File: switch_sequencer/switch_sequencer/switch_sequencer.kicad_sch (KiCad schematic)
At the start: 14 parts, among them SW1 SW_MEC_5G_LED, U4 pico, U5 TMUX4051PWR

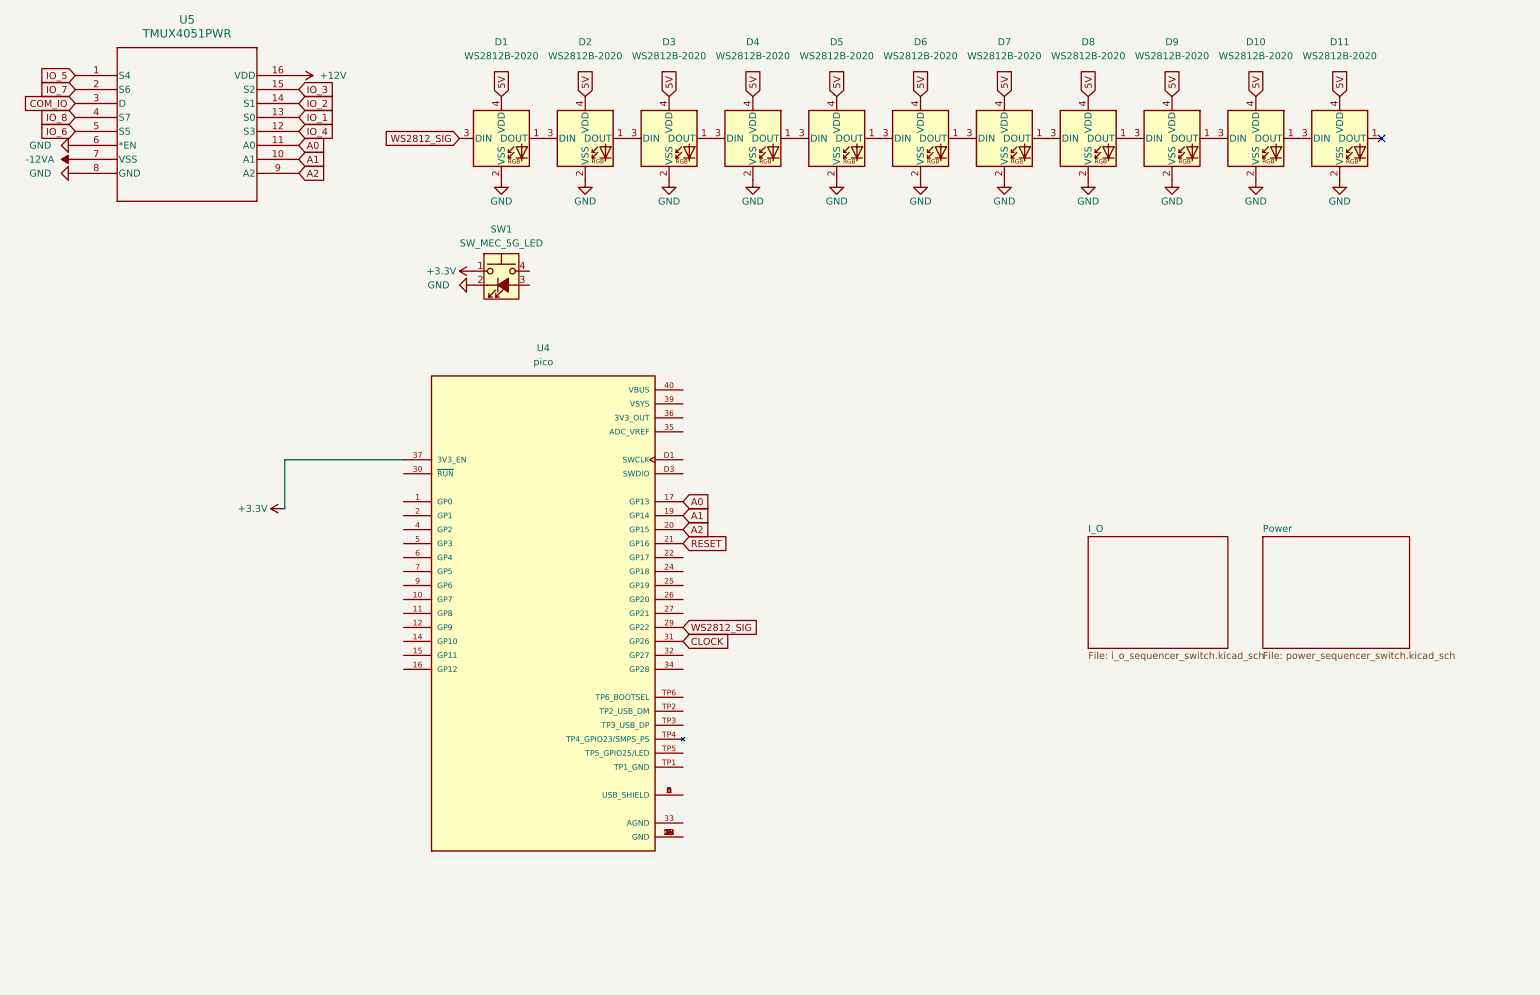
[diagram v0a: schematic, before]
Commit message: Reformated folder structure. Finished layout of sample and hold.
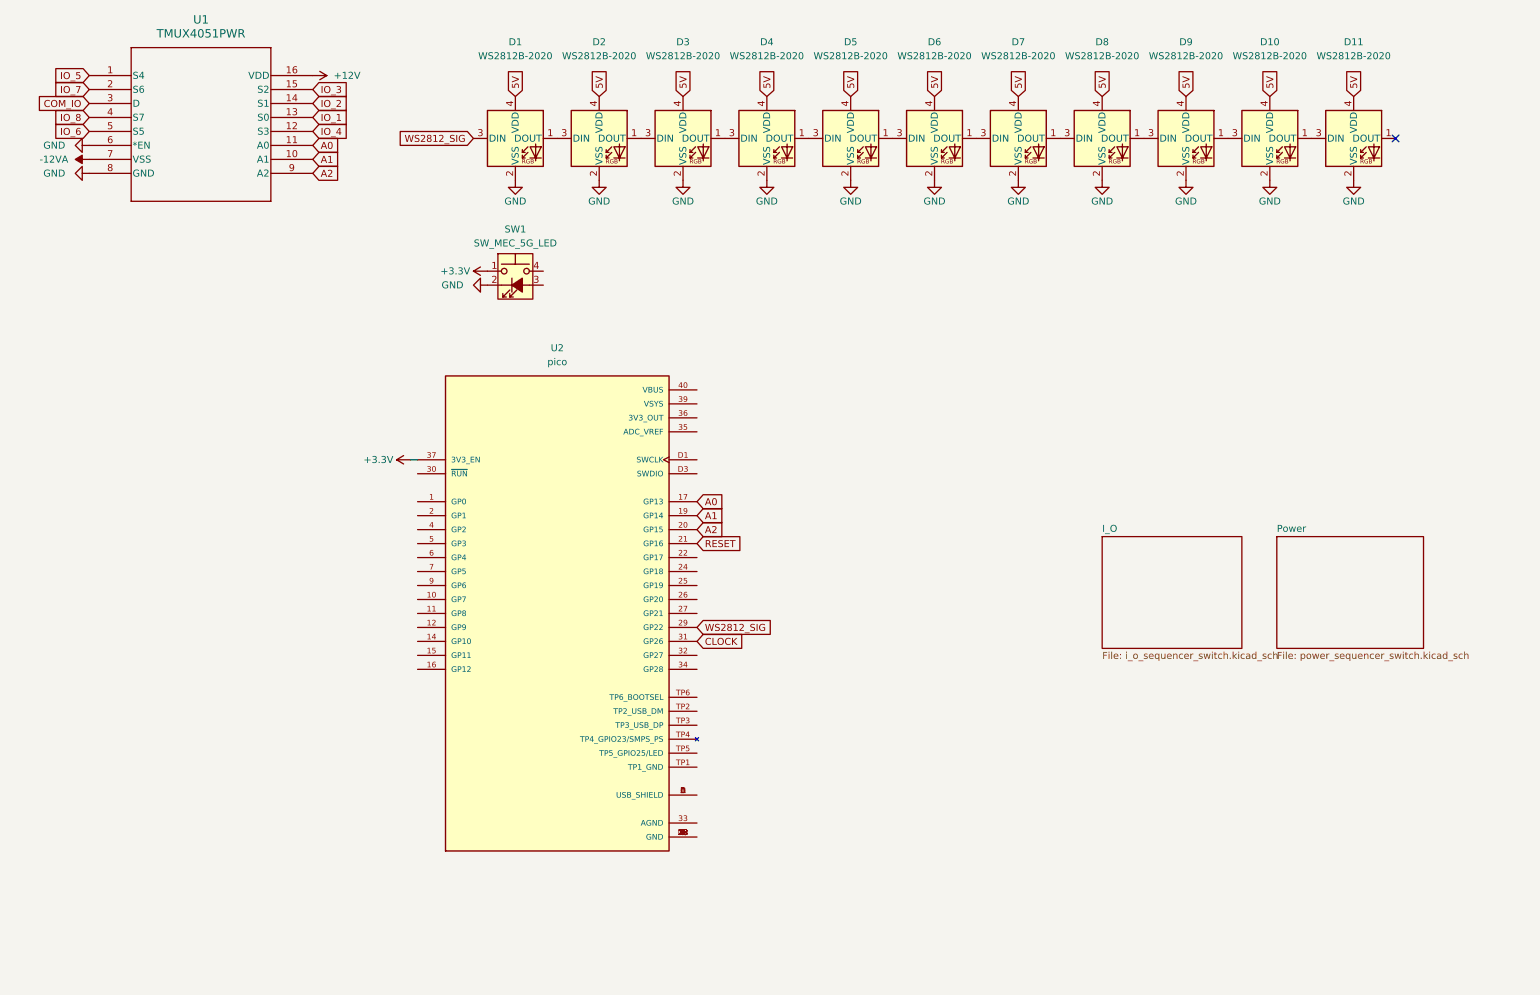
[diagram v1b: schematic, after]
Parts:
- removed U4: pico, SC0915:MODULE_SC0915, symbol pico:pico
- removed U5: TMUX4051PWR, TMUX4051:TSSOP16_PW_TEX, symbol TMUX4051:TMUX4051PWR
- added U1: TMUX4051PWR, TMUX4051:TSSOP16_PW_TEX, symbol TMUX4051:TMUX4051PWR
- added U2: pico, SC0915:MODULE_SC0915, symbol pico:pico
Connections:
- net +12V: now also U1.16 (VDD)
- net +3.3V: now also U2.37 (3V3_EN)
- net -12VA: now also U1.7 (VSS)
- net A0: now also U1.11 (A0), U2.17 (GP13)
- net A1: now also U1.10 (A1), U2.19 (GP14)
- net A2: now also U1.9 (A2), U2.20 (GP15)
- net CLOCK: now also U2.31 (GP26)
- net COM_IO: now also U1.3 (D)
- net GND: now also U1.6 (*EN), U1.8 (GND)
- net IO_1: now also U1.13 (S0)
- net IO_2: now also U1.14 (S1)
- net IO_3: now also U1.15 (S2)
- net IO_4: now also U1.12 (S3)
- net IO_5: now also U1.1 (S4)
- net IO_6: now also U1.5 (S5)
- net IO_7: now also U1.2 (S6)
- net IO_8: now also U1.4 (S7)
- net RESET: now also U2.21 (GP16)
- net WS2812_SIG: now also U2.29 (GP22)
- new net: U2.13 (GND), U2.18 (GND), U2.23 (GND), U2.28 (GND), U2.3 (GND), U2.38 (GND), U2.8 (GND), U2.D2 (GND)
- new net: U2.A (USB_SHIELD), U2.B (USB_SHIELD), U2.C (USB_SHIELD), U2.D (USB_SHIELD)

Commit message: sequential switch wip
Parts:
- removed D1, D10, D11, D2, D3, D4, D5, D6, D7, D8, D9: WS2812B-2020, LED_SMD:LED_WS2812B-2020_PLCC4_2.0x2.0mm, symbol LED:WS2812B-2020
- removed SW1: SW_MEC_5G_LED, symbol Switch:SW_MEC_5G_LED
- removed U1: TMUX4051PWR, TMUX4051:TSSOP16_PW_TEX, symbol TMUX4051:TMUX4051PWR
- removed U2: pico, SC0915:MODULE_SC0915, symbol pico:pico
- added J1, J2: 3.5mm_Mono_Switched_sm, 4ms_Jack:EighthInch_PJ398SM, symbol 4ms_Jack:3.5mm_Mono_Switched_sm
- added J12: Conn_01x03, 4ms_Connector:Pins_1x03_2.54mm_TH, symbol 4ms_Connector:Conn_01x03
- added R1, R2: 1k_0402, 4ms_Resistor:R_0402, symbol 4ms_Resistor:1k_0402
- added U14: Pico, RPi_Pico:RPi_Pico_SMD_TH, symbol MCU_RaspberryPi_and_Boards:Pico
- added U4: TL072, 4ms_Package_SSOP:TSSOP-8_4.4x3mm_Pitch0.65mm, symbol 4ms_IC:TL072
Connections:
- net CLOCK: now also U14.31 (GPIO26_ADC0), U4.1, U4.2 (-)
- net GND: now also J12.2 (Pin_2), U14.38 (GND)
- net RESET: now also U14.32 (GPIO27_ADC1), U4.6 (-), U4.7
- net WS2812_SIG: now also U14.29 (GPIO22)
- new net: J2.1 (SIG), U4.5 (+)
- new net: J1.1 (SIG), R1.1
- new net: R1.2, R2.2, U4.3 (+)
- new net 3V3_OUT: U14.36 (3V3)
- new net ADC_VREF: U14.35 (ADC_VREF), U4.8 (V+)
- new net BUTTON_1: U14.7 (GPIO5)
- new net BUTTON_2: U14.9 (GPIO6)
- new net BUTTON_3: U14.10 (GPIO7)
- new net BUTTON_4: U14.11 (GPIO8)
- new net BUTTON_5: U14.12 (GPIO9)
- new net BUTTON_6: U14.14 (GPIO10)
- new net BUTTON_7: U14.15 (GPIO11)
- new net BUTTON_8: U14.16 (GPIO12)
- new net GNDA: J1.2 (SHEILD), J1.3 (SW), J2.2 (SHEILD), J2.3 (SW), R2.1, U14.33 (AGND), U4.4 (V-)
- new net MUX_D0: U14.17 (GPIO13)
- new net MUX_D1: U14.19 (GPIO14)
- new net MUX_D2: U14.20 (GPIO15)
- new net UART0_RX: J12.3 (Pin_3), U14.2 (GPIO1)
- new net UART0_TX: J12.1 (Pin_1), U14.1 (GPIO0)
- no-connect marks 1 -> 0
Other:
- removed sheet I_O
- added sheet Clock Led (led.kicad_sch)
- added sheet Mux (mux.kicad_sch)
- added sheet Reset Led (led.kicad_sch)
- note added: "For debugging"

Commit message: sequential swtich more wip
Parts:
- added FP1: Top Rail, 4ms_Faceplate:Rail_Connection_16HP, symbol 4ms_Hardware:Faceplate
- added FP2: Bottom Rail, 4ms_Faceplate:Rail_Connection_16HP, symbol 4ms_Hardware:Faceplate
- added Q1: DMG2305UX-7, DMG2305UX_7:SOT91P240X110-3N_DMG2305UX-7, symbol DMG2305UX-7:DMG2305UX-7
- added U2: LM4040DBZ-3, Package_TO_SOT_SMD:SOT-23, symbol Reference_Voltage:LM4040DBZ-3
- U14: footprint RPi_Pico:RPi_Pico_SMD_TH -> MCU_RaspberryPi_and_Boards:RPi_Pico_SMD_TH
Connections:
- net ADC_VREF: now also U2.1 (K)
- net BUTTON_4: no longer U14.11 (GPIO8)
- net BUTTON_5: now also U14.25 (GPIO19); no longer U14.12 (GPIO9)
- net BUTTON_6: now also U14.26 (GPIO20); no longer U14.14 (GPIO10)
- net BUTTON_7: now also U14.27 (GPIO21); no longer U14.15 (GPIO11)
- net BUTTON_8: now also U14.29 (GPIO22); no longer U14.16 (GPIO12)
- net GNDA: now also U2.2 (A)
- net WS2812_SIG: no longer U14.29 (GPIO22)
- net at U14.39 (VSYS): now also Q1.2
- net at U14.40 (VBUS): now also Q1.1
- new net 5V: Q1.3
- no-connect marks 0 -> 1

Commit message: sequential switch wip more more
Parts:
- removed FP1: Top Rail, 4ms_Faceplate:Rail_Connection_16HP, symbol 4ms_Hardware:Faceplate
- removed FP2: Bottom Rail, 4ms_Faceplate:Rail_Connection_16HP, symbol 4ms_Hardware:Faceplate
- added H1, H2, H3, H4: MountingHole, 4ms_Faceplate:Faceplate_Rail_Mount_Slot_Plated, symbol Mechanical:MountingHole
- added SW9: D6R90F2LFS, D6R90:D6R90_CNK, symbol D6R90:D6R90F2LFS
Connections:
- net BUTTON_1: now also U14.16 (GPIO12); no longer U14.7 (GPIO5)
- net BUTTON_2: now also U14.15 (GPIO11); no longer U14.9 (GPIO6)
- net BUTTON_3: now also U14.14 (GPIO10); no longer U14.10 (GPIO7)
- net BUTTON_4: now also U14.12 (GPIO9)
- net CLOCK: now also U14.32 (GPIO27_ADC1); no longer U14.31 (GPIO26_ADC0)
- net GND: now also SW9.2
- net RESET: now also U14.31 (GPIO26_ADC0); no longer U14.32 (GPIO27_ADC1)
- net WS2812_SIG: now also U14.22 (GPIO17)
- net BUTTON_9: now reaches U14.21 (GPIO16)
- net BUTTON_9: now also SW9.1
- no-connect marks 1 -> 20
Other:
- added sheet Mode Led (led.kicad_sch)
